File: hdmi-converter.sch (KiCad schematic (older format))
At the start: 107 parts, among them J2 46756-1001, Q1 BSS138APW, Q2 BSS138APW, Q3 BSS138APW, Q4 BSS138APW, U2 LT9611, U3 TXB0104RUT, U4 NTS0102GT, Y2 ABM8G-24.000MHZ-18-D2Y-T

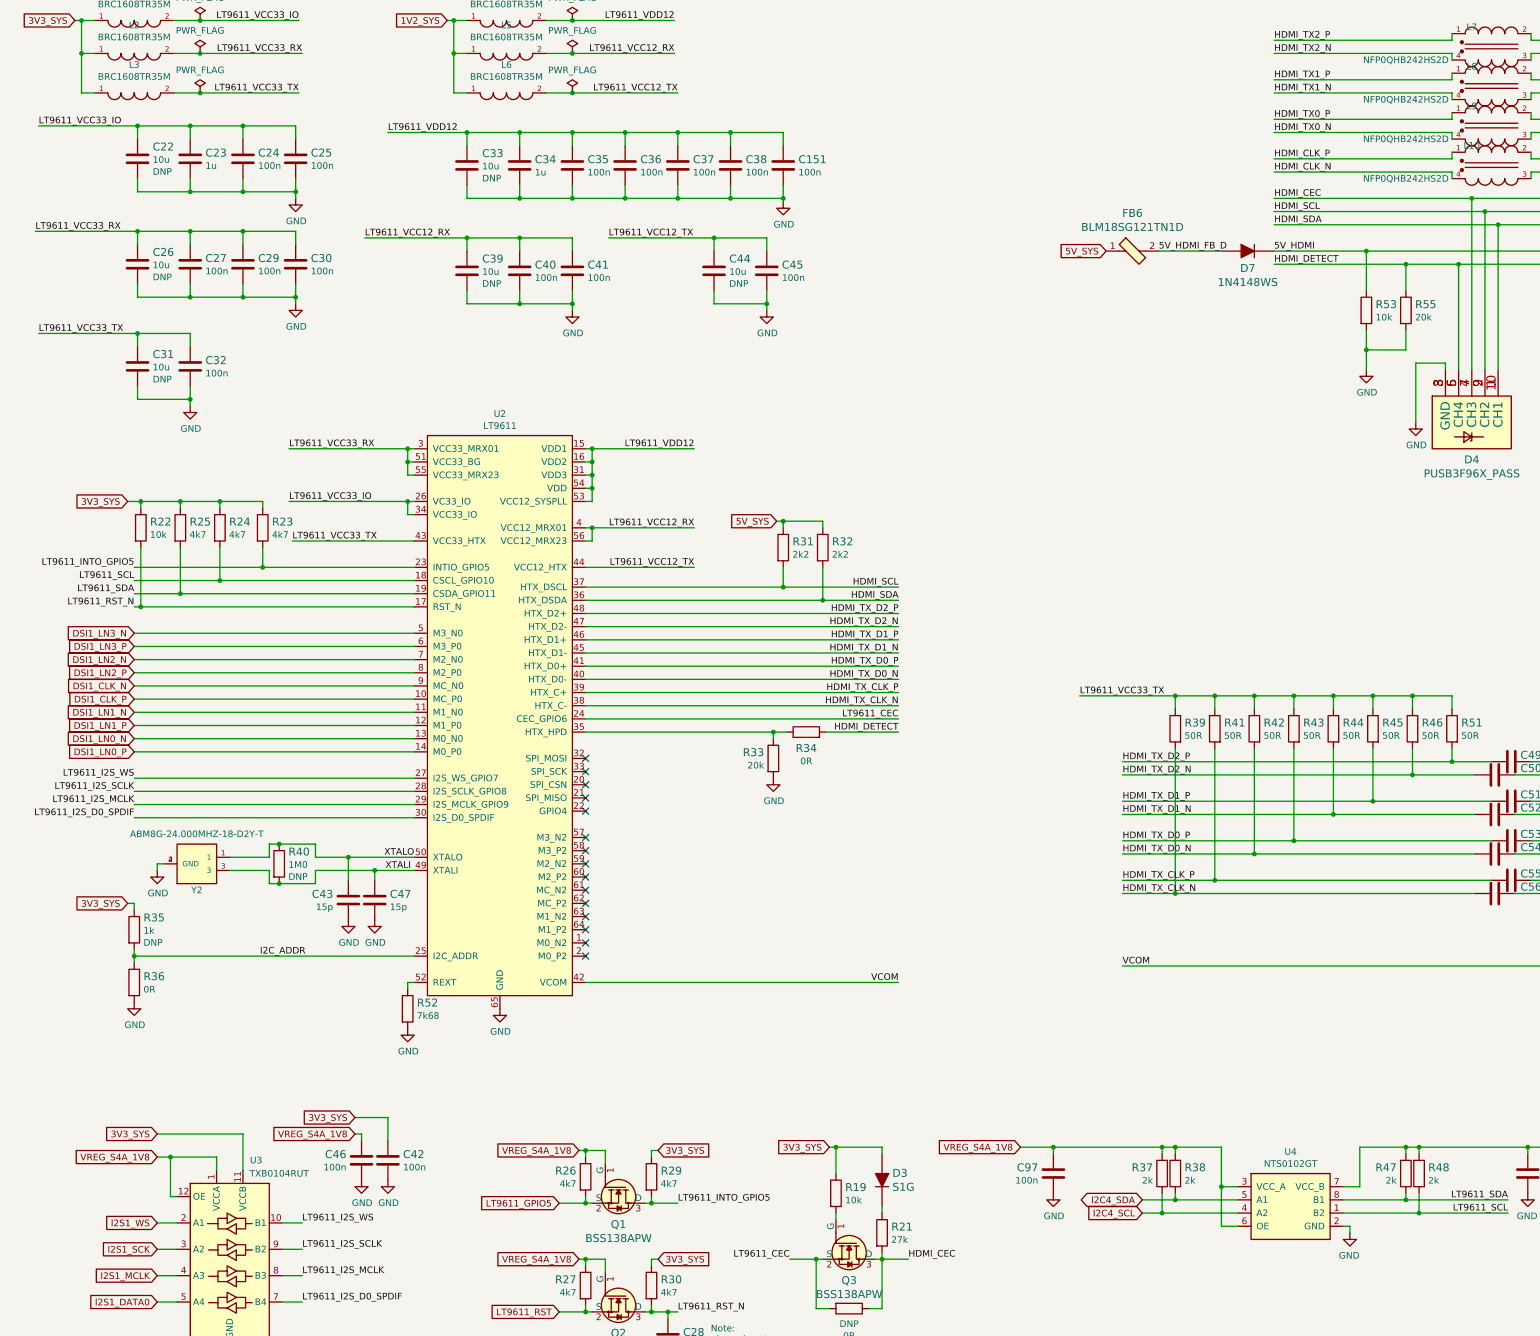
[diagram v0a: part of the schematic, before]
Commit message: Add test points
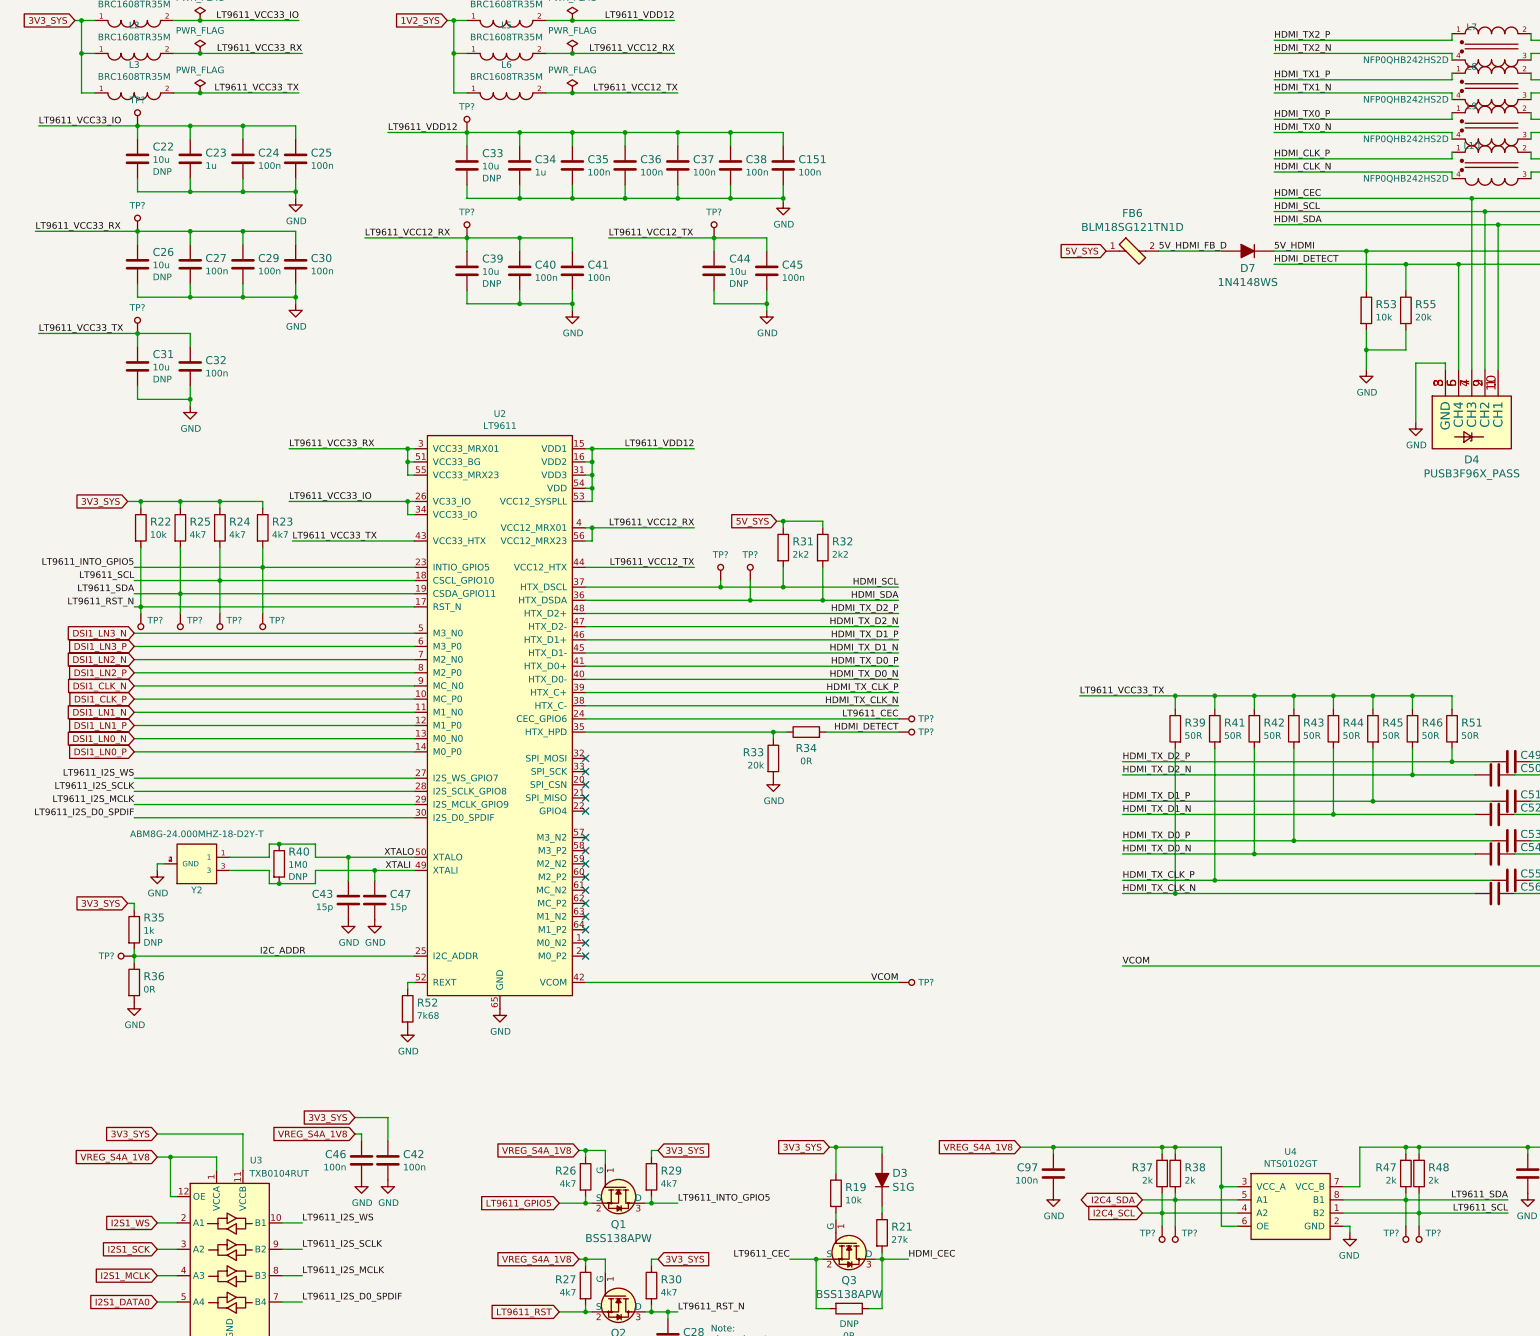
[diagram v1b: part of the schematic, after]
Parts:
- added TP? (x20): TP_SMD_0_75MM, antmicro-footprints:Testpoint_smd_0_75mm, symbol antmicroTestPoints:TP_SMD_0_75MM
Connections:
- net HDMI_DETECT: now also TP?.1
- net HDMI_SCL: now also TP?.1
- net HDMI_SDA: now also TP?.1
- net I2C4_SCL: now also TP?.1
- net I2C4_SDA: now also TP?.1
- net I2C_ADDR: now also TP?.1
- net LT9611_CEC: now also TP?.1
- net LT9611_INTO_GPIO5: now also TP?.1
- net LT9611_RST_N: now also TP?.1
- net LT9611_SCL: now also TP?.1, TP?.1
- net LT9611_SDA: now also TP?.1, TP?.1
- net LT9611_VCC12_RX: now also TP?.1
- net LT9611_VCC12_TX: now also TP?.1
- net LT9611_VCC33_IO: now also TP?.1
- net LT9611_VCC33_RX: now also TP?.1
- net LT9611_VCC33_TX: now also TP?.1
- net LT9611_VDD12: now also TP?.1
- net VCOM: now also TP?.1

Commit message: Annotate test points, reimport 510R from global library
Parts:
- R134, R137, R58, R60, R61, R62, R87: symbol sa800u-baseboard-hw:R_510R_0402 -> antmicroResistors0402:R_510R_0402
- R?: renamed from R57; symbol sa800u-baseboard-hw:R_510R_0402 -> antmicroResistors0402:R_510R_0402
- R?: renamed from R52; symbol sa800u-baseboard-hw:R_7k68_0402 -> antmicroResistors0402:R_7k68_0402
- gave numbers to parts that had none: 20

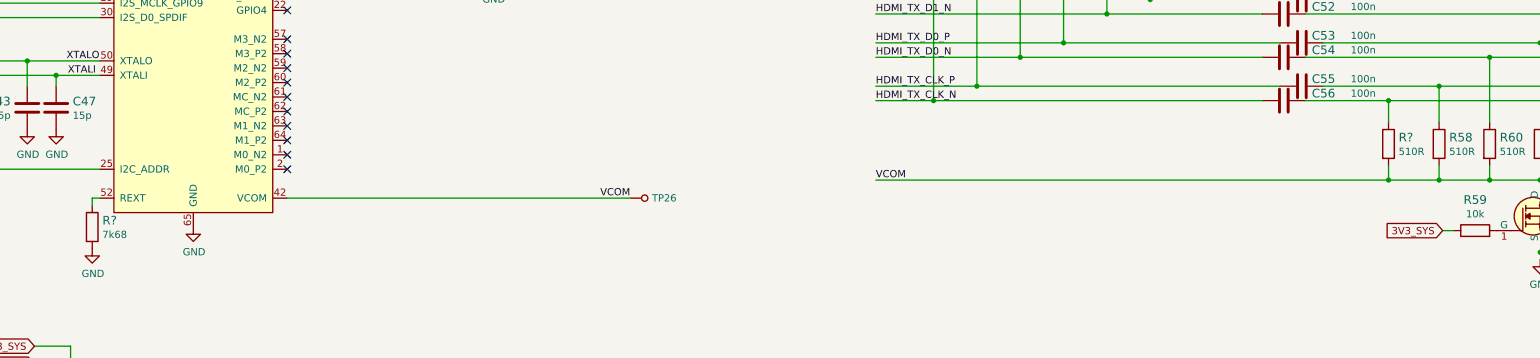
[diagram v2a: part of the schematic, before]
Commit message: Fix labels, fix p-mosfet symbol
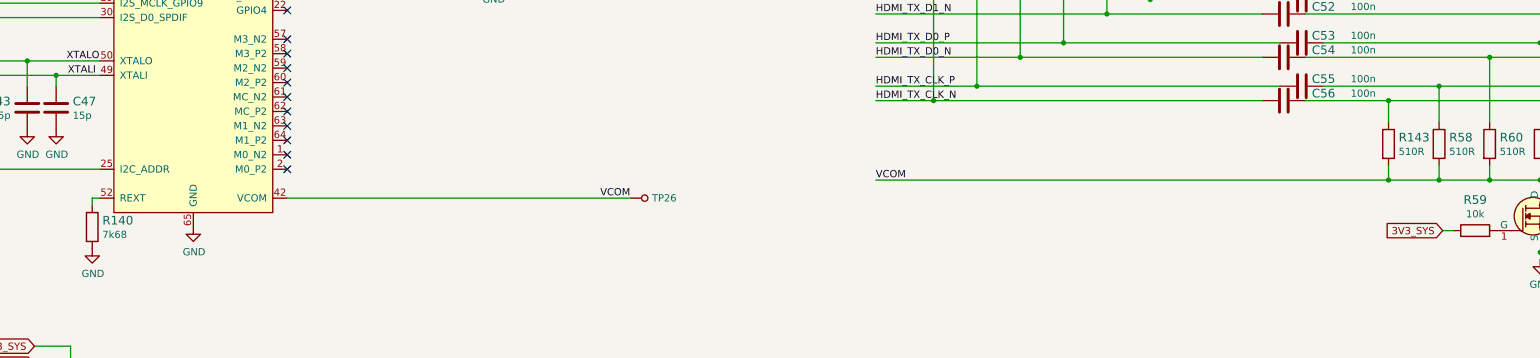
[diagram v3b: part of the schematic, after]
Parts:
- gave numbers to parts that had none: 2
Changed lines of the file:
@@
 	11025 9925 11025 9725
 $Comp
-L antmicroResistors0402:R_7k68_0402 R?
+L antmicroResistors0402:R_7k68_0402 R140
 U 1 1 629B0277
 P 3450 8275
-F 0 "R?" V 3405 8345 60  0000 L CNN
+F 0 "R140" V 3405 8345 60  0000 L CNN
 F 1 "R_7k68_0402" H 3450 8125 60  0001 C CNN
 F 2 "sa800u-baseboard-hw-footprints:0402-res" H 3650 8475 60  0001 L CNN
@@
 $EndComp
 $Comp
-L antmicroResistors0402:R_510R_0402 R?
+L antmicroResistors0402:R_510R_0402 R143
 U 1 1 622FF01E
 P 12425 7700
-F 0 "R?" V 12380 7770 60  0000 L CNN
+F 0 "R143" V 12380 7770 60  0000 L CNN
 F 1 "R_510R_0402" H 12425 7550 60  0001 C CNN
 F 2 "sa800u-baseboard-hw-footprints:0402-res" H 12625 7900 60  0001 L CNN
